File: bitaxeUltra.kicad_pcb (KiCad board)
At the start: 4 copper layers, 106.8 x 106.8 mm, 141 parts, among them J1 54-00164, J2 Conn_01x02, J3 Conn_01x05, J4 Conn_01x04, J5 TC2030-IDC, J7 Conn_01x02, J8 USB_C_Receptacle_USB2.0, J9 Conn_01x04, Q1 CSD17311Q5, Q2 CSD17311Q5, Q4 2N7002K, SW1 GT-TC029B-H025-L1N, SW2 GT-TC029B-H025-L1N, U1 25MHz, U10 DS4432U+, U11 RT9080-33GJ5, U12 ESP32-S3-WROOM-1, U14 BM1366_mode1, U2 TXB0104RGYR, U5 MCP1824T-1802E, U6 MCP1824T-0802E, U7 EMC2101, U8 INA260, U9 TPS40305, Y1 32.768kHz

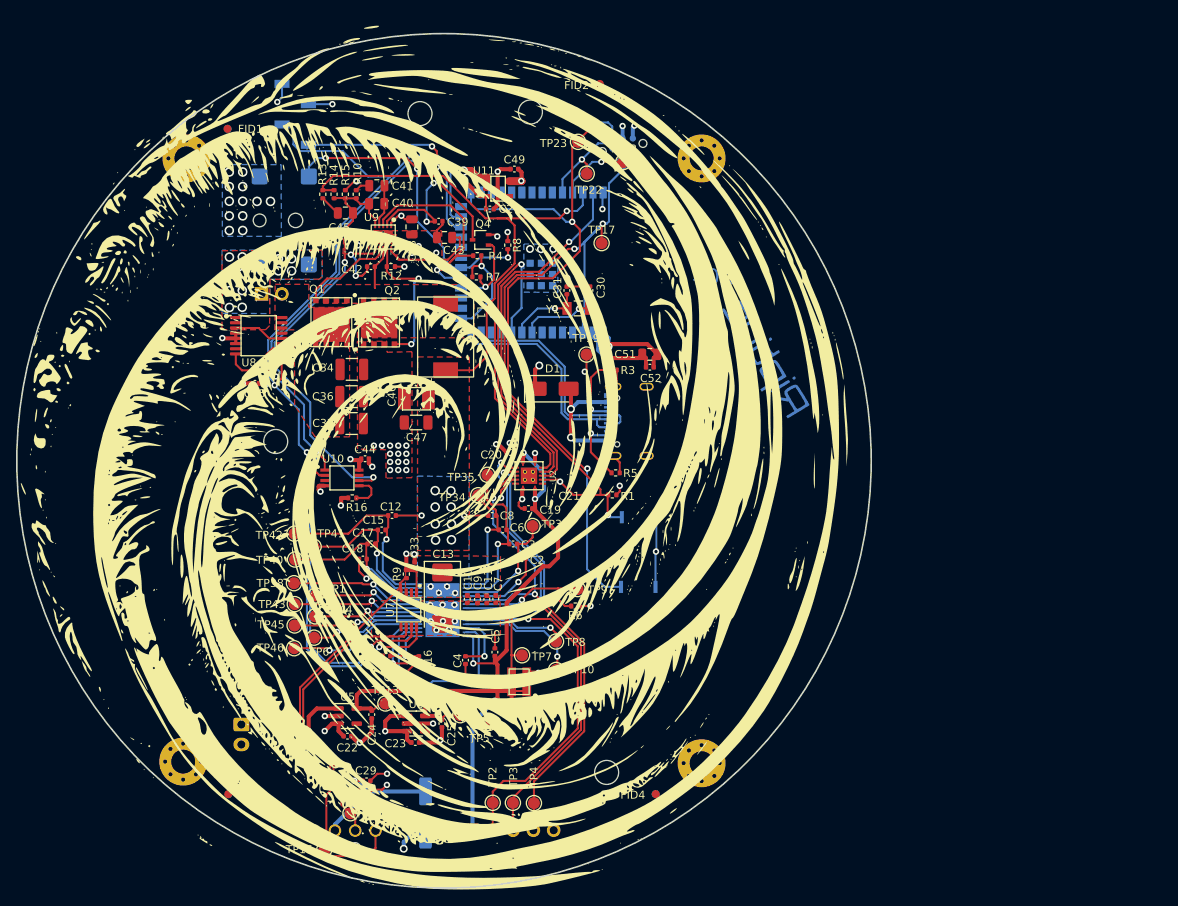
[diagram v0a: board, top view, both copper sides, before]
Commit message: Update: moved power, buttons and adapted screen for OLED Yellow and Blue Screen
Update: moved power, buttons and adapted screen for OLED Yellow and Blue Screen
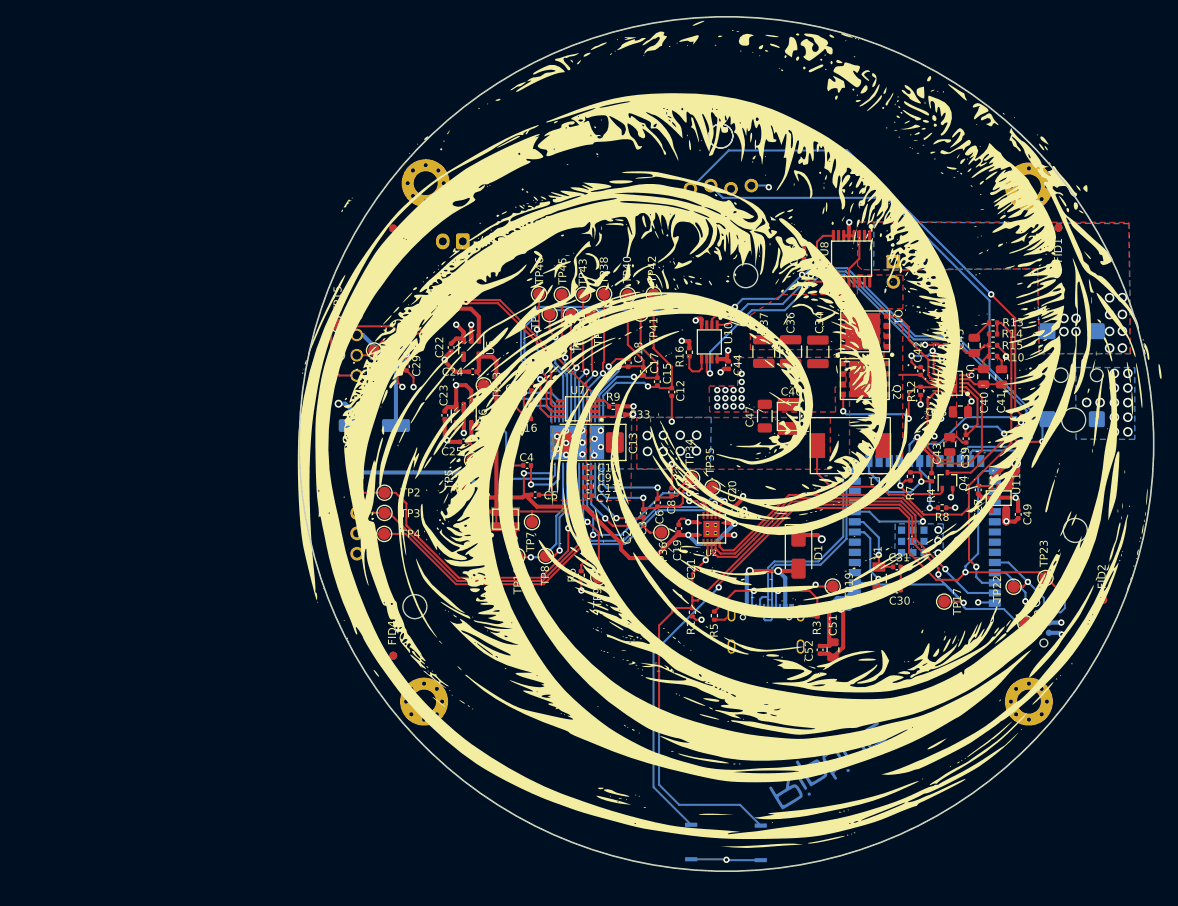
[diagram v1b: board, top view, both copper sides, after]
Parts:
- removed J9: Conn_01x04, Connector_PinSocket_2.54mm:PinSocket_1x04_P2.54mm_Vertical_SMD_Pin1Right
- added ? (x2): , , F.Cu at (140.4, 56.8)
- added J3: Conn_01x04, bitaxe:PinHeader_1x04_P2.54mm_Vertical_shifted, B.Cu at (136.6, 63.2)
- moved H8 105.4 mm to (178.9, 63.1), turned to -90 degrees
- moved FID1 104.6 mm to (182.6, 68.2), turned to -90 degrees
- moved FID6 104.6 mm to (182.6, 68.2), turned to 90 degrees
- moved J1 100.4 mm to (184.3, 86.7), turned to -90 degrees
- moved ? 90.2 mm to (184.5, 92.3), turned to -90 degrees
- moved FID2 90.1 mm to (188.2, 114.8), turned to -90 degrees
- moved FID5 90.1 mm to (188.2, 114.8), turned to 90 degrees
- moved ? 85.9 mm to (184.7, 106.1), turned to -90 degrees
- moved R13 85.3 mm to (174.4, 80.1), turned to 180 degrees
- moved R14 84.2 mm to (174.4, 81.6), turned to 180 degrees
- moved R15 83.1 mm to (174.4, 83.0), turned to 0 degrees
- moved R10 82.1 mm to (174.4, 84.3), turned to 180 degrees
- moved C41 81.7 mm to (175.5, 86.9), turned to 90 degrees
- moved C45 80.3 mm to (172.1, 83.0), turned to -90 degrees
- moved TP23 79.9 mm to (181.0, 112.1), turned to -90 degrees
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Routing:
- net /SDA: track 128.0 -> 175.6 mm
- net /3V3: track 74.3 -> 121.4 mm, vias 15 -> 14
- net /SCL: track 126.5 -> 162.9 mm
- net /ESP32/EN: track 81.0 -> 116.7 mm
- net /ESP32/IO0: track 92.0 -> 109.3 mm
- net /PLUG_SENSE: track 38.4 -> 32.4 mm
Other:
- board text removed: "204"
